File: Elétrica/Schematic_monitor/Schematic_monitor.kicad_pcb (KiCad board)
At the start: 2 copper layers, 49 parts, among them J1 Conn_01x04, J2 USB_B_Micro, J3 Eletrode 1, J4 Eletrode 2, SW1 SW_Push, SW2 SW_SPDT, SW3 SW_SPDT, SW4 SW_SPDT, SW5 SW_SPDT, SW6 SW_SPDT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

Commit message: Temp sensor
Adicionado sensor de temperatura
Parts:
- removed SW3, SW4, SW5, SW6, SW7: SW_SPDT, Button_Switch_SMD:SW_DIP_SPSTx01_Slide_9.78x4.72mm_W8.61mm_P2.54mm
- removed U3: EA_eDIPTFT32-A, Display:EA_eDIPTFT32-XXX
- C15: footprint Capacitor_SMD:C_Elec_3x5.4 -> Capacitor_SMD:C_0603_1608Metric_Pad1.08x0.95mm_HandSolder
- FB1, FB3: value FerriteBead -> New_Library:FerriteBead; footprint Inductor_SMD:L_0603_1608Metric -> Inductor_SMD:L_0603_1608Metric_Pad1.05x0.95mm_HandSolder
- FB2: footprint Inductor_SMD:L_0603_1608Metric -> Inductor_SMD:L_0603_1608Metric_Pad1.05x0.95mm_HandSolder
- moved U4 40.5 mm to (142.2, 91.4)
- moved D3 8.79 mm to (131.8, 119.0)
- moved C15 3.50 mm to (121.9, 123.2)
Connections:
- U1 pad 16: ADC1-2 -> unconnected-(U1-PA2-Pad16)
- U1 pad 41: unconnected-(U1-PA8-Pad41) -> I2C3_SCL
- U1 pad 42: unconnected-(U1-PA9-Pad42) -> I2C3_SDA
- U1 pad 58: unconnected-(U1-PB6-Pad58) -> I2C1_SCL
- U1 pad 59: unconnected-(U1-PB7-Pad59) -> I2C1_SDA
- U4 pad 2: unconnected-(U4-SCL-Pad2) -> I2C3_SCL
- U4 pad 3: unconnected-(U4-SDA-Pad3) -> I2C3_SDA

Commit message: sensor de temperatura
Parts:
- added C18: 0.1uF, Capacitor_SMD:C_0603_1608Metric, F.Cu at (159.4, 96.8)
- added U3: MLX90614ESF-ACC-000-TU, footprints:MLX90614xCC_MEL, F.Cu at (161.5, 87.8)
- D3: footprint Diode_SMD:D_PowerDI-5 -> Diode_SMD:D_0603_1608Metric
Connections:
- U1 pad 53: unconnected-(U1-PC12-Pad53) -> I2C1_SDA

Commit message: Atualizações
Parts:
- added U5: AD623, AD623:RM_8_ADI-L, F.Cu at (131.2, 103.2)
- added U6: LM358, LM358:D8-L, F.Cu at (138.3, 100.8)
- added U7: LM358, LM358:D8-L, F.Cu at (138.3, 107.3)
- added U8: LM358, LM358:D8-L, F.Cu at (138.3, 113.7)
- J3, J4: footprint Connector_PinHeader_1.00mm:PinHeader_1x01_P1.00mm_Horizontal -> Connector_PinHeader_2.54mm:PinHeader_1x01_P2.54mm_Vertical
- U3: footprint footprints:MLX90614xCC_MEL -> temp:MLX90614xCC_MEL
- U4: footprint oxy:21-0880B_MXM -> oximeter:21-0880B_MXM-L
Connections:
- net I2C1_SCL renamed scl_lcd
- C18 pad 1: VBUS -> GND
- C18 pad 2: GND -> VBUS
- J3 pad 1: Net-(J3-Pin_1) -> /EMG
- U1 pad 29: unconnected-(U1-PB10-Pad29) -> Temp_SCL
- U1 pad 41: I2C3_SCL -> oxi_scl
- U1 pad 42: I2C3_SDA -> oxi_sda
- U1 pad 53: I2C1_SDA -> Temp_SDA
- U1 pad 59: I2C1_SDA -> sda_lcd
- U3 pad 1: I2C3_SCL -> Temp_SCL
- U3 pad 2: I2C3_SDA -> Temp_SDA
- U3 pad 3: GND -> VBUS
- U4 pad 2: I2C3_SCL -> oxi_scl
- U4 pad 3: I2C3_SDA -> oxi_sda

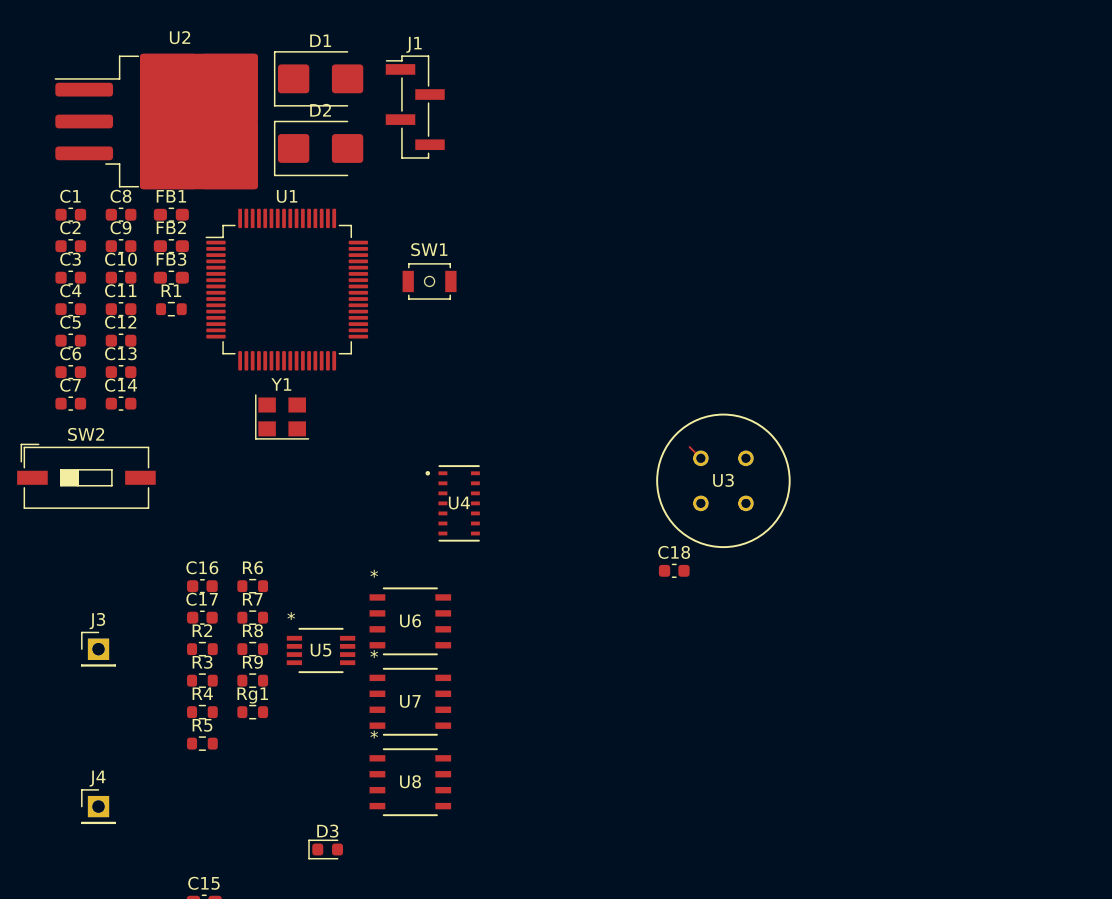
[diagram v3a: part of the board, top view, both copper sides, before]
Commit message: Versão PRJ2 e PRJ3 quase finalizada
Poucos detalhes precisam ser alterados para o envio dos trabalhos pelo menos do PRJ2. PRJ3 está finalizado
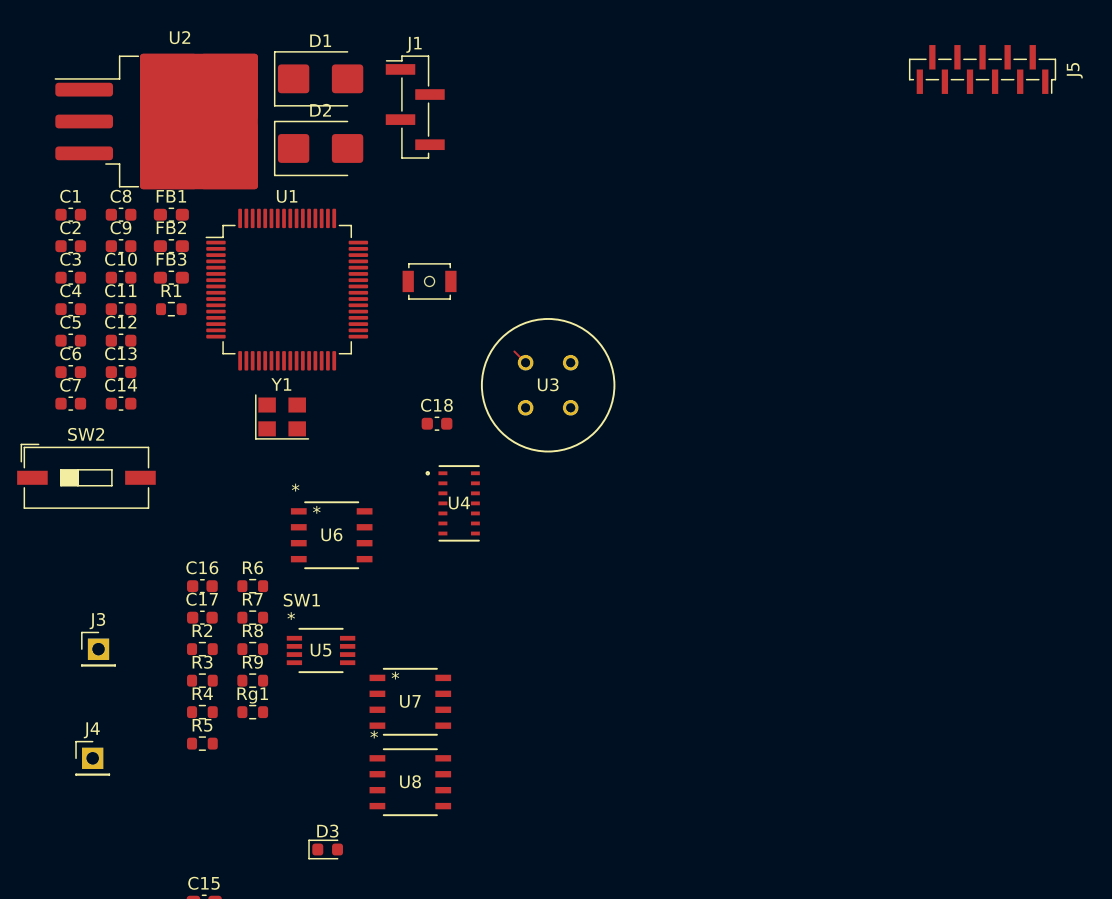
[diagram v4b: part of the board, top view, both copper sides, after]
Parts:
- added J5: Conn_01x11, Connector_PinSocket_1.00mm:PinSocket_1x11_P1.00mm_Vertical_SMD_Pin1Right, F.Cu at (184.0, 56.9)
- moved C18 22.3 mm to (140.5, 85.1)
- moved U3 15.9 mm to (147.5, 80.2)
- moved U6 9.30 mm to (132.1, 94.0)
- moved J4 3.88 mm to (113.0, 111.8)
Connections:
- U1 pad 14: ADC1-0 -> unconnected-(U1-PA0-Pad14)
- U1 pad 20: unconnected-(U1-PA4-Pad20) -> touch_int
- U1 pad 21: unconnected-(U1-PA5-Pad21) -> displ_sck
- U1 pad 22: unconnected-(U1-PA6-Pad22) -> touch_mosi
- U1 pad 23: unconnected-(U1-PA7-Pad23) -> displ_mosi
- U1 pad 33: unconnected-(U1-PB12-Pad33) -> displ_cs
- U1 pad 34: unconnected-(U1-PB13-Pad34) -> touch_cs
- U1 pad 35: unconnected-(U1-PB14-Pad35) -> displ_dc
- U1 pad 36: unconnected-(U1-PB15-Pad36) -> displ_rst
- U1 pad 38: unconnected-(U1-PC7-Pad38) -> displ_led

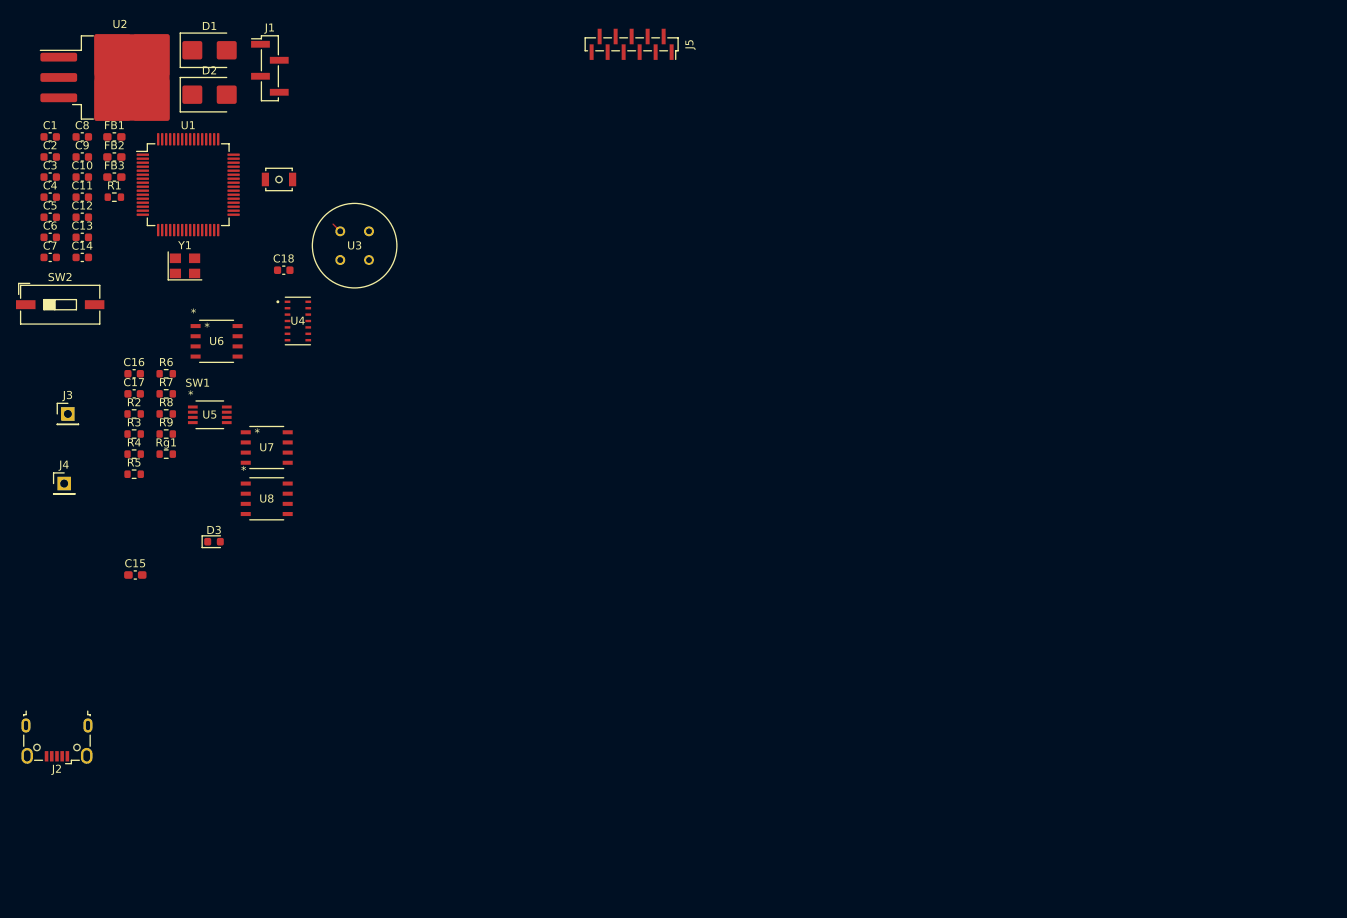
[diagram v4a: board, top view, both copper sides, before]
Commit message: Final Detalis to  PRJ2
Added final detalis in PCB desing and STM32 configuration.
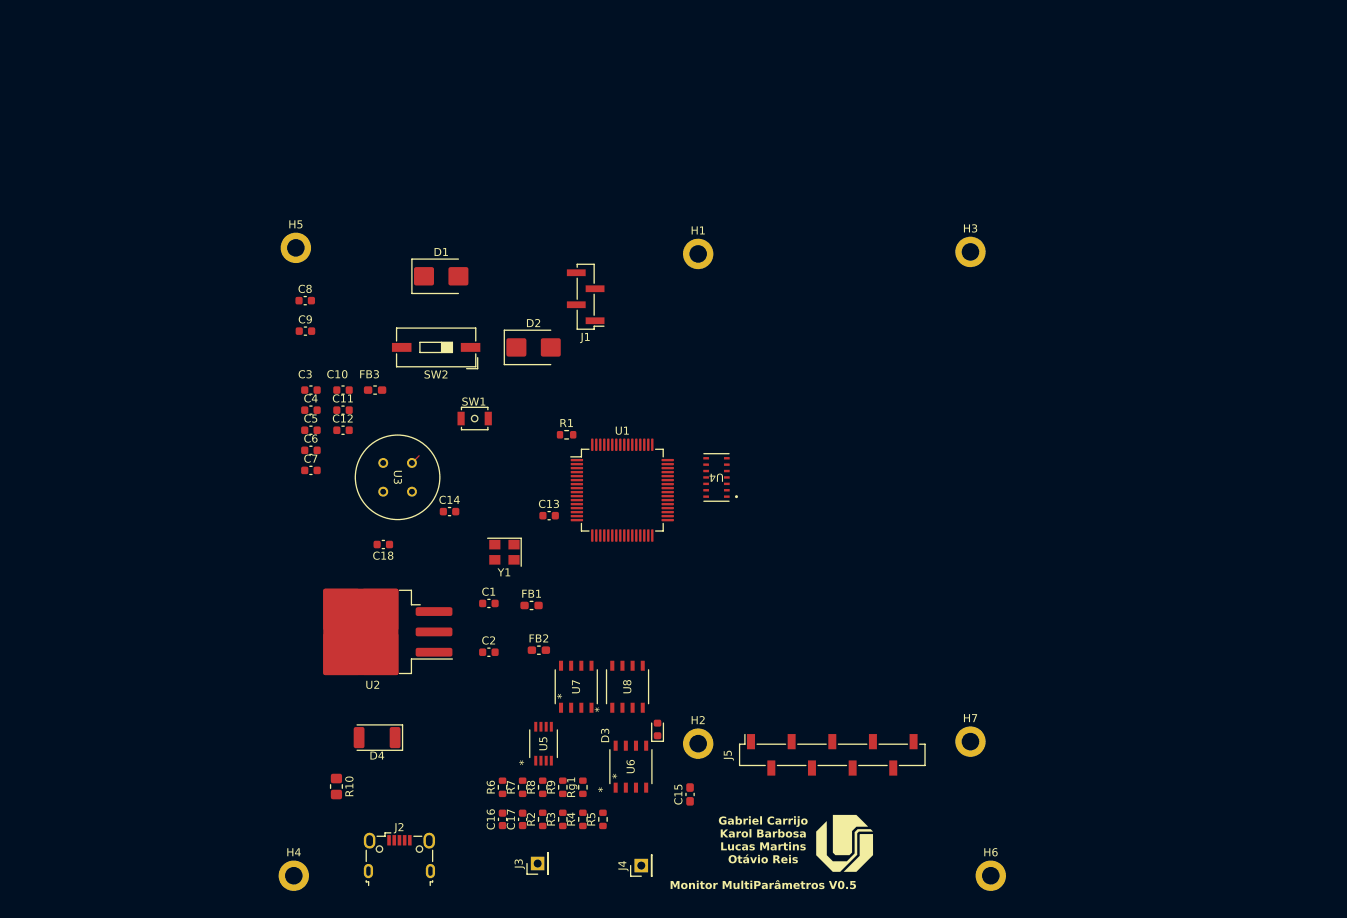
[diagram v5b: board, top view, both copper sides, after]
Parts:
- added D4: LED, LED_SMD:LED_2010_5025Metric, F.Cu at (152.1, 143.5)
- added G***: LOGO, UFU_bitmapfile:UFU_Bitmap, F.Cu at (210.6, 156.7)
- added H1: MountingHole_Pad, MountingHole:MountingHole_2.2mm_M2_DIN965_Pad, F.Cu at (192.3, 83.1)
- added H2: MountingHole_Pad, MountingHole:MountingHole_2.2mm_M2_DIN965_Pad, F.Cu at (192.3, 144.3)
- added H3: MountingHole_Pad, MountingHole:MountingHole_2.2mm_M2_DIN965_Pad, F.Cu at (226.3, 82.8)
- added H4: MountingHole_Pad, MountingHole:MountingHole_2.2mm_M2_DIN965_Pad, F.Cu at (141.7, 160.8)
- added H5: MountingHole_Pad, MountingHole:MountingHole_2.2mm_M2_DIN965_Pad, F.Cu at (142.0, 82.3)
- added H6: MountingHole_Pad, MountingHole:MountingHole_2.2mm_M2_DIN965_Pad, F.Cu at (228.9, 160.8)
- added H7: MountingHole_Pad, MountingHole:MountingHole_2.2mm_M2_DIN965_Pad, F.Cu at (226.3, 144.0)
- added R10: 100, Resistor_SMD:R_0805_2012Metric_Pad1.20x1.40mm_HandSolder, F.Cu at (147.1, 149.6)
- J5: value Conn_01x11 -> Conn_01x09; footprint Connector_PinSocket_1.00mm:PinSocket_1x11_P1.00mm_Vertical_SMD_Pin1Right -> Connector_PinSocket_2.54mm:PinSocket_1x09_P2.54mm_Vertical_SMD_Pin1Right
- moved J5 92.3 mm to (209.0, 145.7), turned to 90 degrees
- moved J4 86.5 mm to (185.2, 159.5), turned to 90 degrees
- moved C2 82.7 mm to (166.1, 132.8)
- moved FB2 81.3 mm to (172.4, 132.6)
- moved J3 81.3 mm to (172.2, 159.3), turned to 90 degrees
- moved C1 80.0 mm to (166.1, 126.7)
- moved FB1 78.4 mm to (171.4, 127.0)
- moved U2 76.2 mm to (151.6, 130.3), turned to 180 degrees
- moved C15 74.6 mm to (191.3, 150.6), turned to 90 degrees
- moved U6 74.2 mm to (183.9, 147.1), turned to 90 degrees
- moved R5 72.8 mm to (180.4, 153.7), turned to 90 degrees
- moved R4 72.3 mm to (177.9, 153.7), turned to 90 degrees
- moved C16 72.3 mm to (167.8, 153.7), turned to 90 degrees
- moved R3 72.0 mm to (175.4, 153.7), turned to 90 degrees
- moved C17 72.0 mm to (170.3, 153.7), turned to 90 degrees
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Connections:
- C15 pad 1: Net-(C15-Pad1) -> ADC1-1
- C15 pad 2: Net-(U7A-+) -> ADC1-1
- C16 pad 1: Net-(C16-Pad1) -> ADC1-1
- C16 pad 2: Vref -> ADC1-1
- C17 pad 1: Net-(C16-Pad1) -> ADC1-1
- C17 pad 2: Net-(U8A--) -> ADC1-1
- J3 pad 1: /EMG -> ADC1-1
- J4 pad 1: Net-(J4-Pin_1) -> ADC1-1
- J5 pad 1: GND -> displ_led
- J5 pad 2: displ_led -> displ_rst
- J5 pad 3: displ_rst -> displ_dc
- J5 pad 4: displ_dc -> touch_cs
- J5 pad 5: touch_cs -> displ_cs
- J5 pad 6: displ_cs -> displ_mosi
- J5 pad 7: displ_mosi -> touch_mosi
- J5 pad 8: touch_mosi -> displ_sck
- J5 pad 9: displ_sck -> touch_int
- R2 pad 2: Net-(U6A-+) -> ADC1-1
- R3 pad 1: Net-(U6A-+) -> ADC1-1
- R4 pad 1: Net-(U7A-+) -> ADC1-1
- R4 pad 2: Vref -> ADC1-1
- R5 pad 1: Net-(R5-Pad1) -> ADC1-1
- R5 pad 2: Net-(U7A--) -> ADC1-1
- R6 pad 1: Net-(U7A--) -> ADC1-1
- R7 pad 1: Net-(R5-Pad1) -> ADC1-1
- R7 pad 2: Net-(C16-Pad1) -> ADC1-1
- R8 pad 1: Net-(C16-Pad1) -> ADC1-1
- R8 pad 2: Net-(U8A-+) -> ADC1-1
- R9 pad 1: Net-(U8A--) -> ADC1-1
- Rg1 pad 1: Net-(Rg1-Pad1) -> ADC1-1
- U5 pad 1: Net-(Rg1-Pad1) -> ADC1-1
- U5 pad 2: /EMG -> ADC1-1
- U5 pad 3: Net-(J4-Pin_1) -> ADC1-1
- U5 pad 5: Vref -> ADC1-1
- U5 pad 6: Net-(C15-Pad1) -> ADC1-1
- U6 pad 1: Vref -> ADC1-1
- U6 pad 2: Vref -> ADC1-1
- U6 pad 3: Net-(U6A-+) -> ADC1-1
- U7 pad 1: Net-(R5-Pad1) -> ADC1-1
- U7 pad 2: Net-(U7A--) -> ADC1-1
- U7 pad 3: Net-(U7A-+) -> ADC1-1
- U8 pad 1: Net-(U8A--) -> ADC1-1
- U8 pad 2: Net-(U8A--) -> ADC1-1
- U8 pad 3: Net-(U8A-+) -> ADC1-1
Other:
- board text added: "Gabriel Carrijo Karol Barbosa Lucas Martins Otávio Reis Monitor MultiParâmetros V0.5"

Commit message: Inicio PRJ4
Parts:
- D1, D2: footprint Diode_SMD:D_SMB -> Diode_SMD:D_0603_1608Metric_Pad1.05x0.95mm_HandSolder
- H2: value MountingHole_Pad -> ~
- moved J2 81.5 mm to (183.1, 81.7)
- moved D4 75.1 mm to (226.8, 150.8)
- moved R10 74.3 mm to (221.4, 151.1)
- moved U2 60.0 mm to (208.1, 110.1)
- moved U4 49.3 mm to (185.9, 159.6), turned to 0 degrees
- moved Y1 41.4 mm to (207.2, 133.7)
- moved U7 36.8 mm to (143.5, 152.4), turned to 180 degrees
- moved R5 35.7 mm to (144.8, 156.5), turned to 180 degrees
- moved C13 35.1 mm to (206.7, 127.6)
- moved C15 34.2 mm to (157.2, 153.6)
- moved U6 33.6 mm to (153.0, 160.3), turned to 0 degrees
- moved D3 31.7 mm to (155.5, 142.8), turned to 0 degrees
- moved U8 29.7 mm to (155.4, 147.1), turned to 0 degrees
- moved FB1 28.7 mm to (200.1, 129.5)
- moved FB2 28.7 mm to (201.0, 135.1)
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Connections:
- C15 pad 1: ADC1-1 -> Net-(C15-Pad1)
- C15 pad 2: ADC1-1 -> Net-(U7A-+)
- C16 pad 1: ADC1-1 -> Net-(C16-Pad1)
- C16 pad 2: ADC1-1 -> Vref
- C17 pad 1: ADC1-1 -> Net-(C16-Pad1)
- C17 pad 2: ADC1-1 -> Net-(U8A--)
- J3 pad 1: ADC1-1 -> Net-(J3-Pin_1)
- J4 pad 1: ADC1-1 -> Net-(J4-Pin_1)
- R2 pad 2: ADC1-1 -> Net-(U6A-+)
- R3 pad 1: ADC1-1 -> GND
- R4 pad 1: ADC1-1 -> Net-(U7A-+)
- R4 pad 2: ADC1-1 -> Vref
- R5 pad 1: ADC1-1 -> Net-(R5-Pad1)
- R5 pad 2: ADC1-1 -> Net-(U7A--)
- R6 pad 1: ADC1-1 -> Net-(U7A--)
- R7 pad 1: ADC1-1 -> Net-(R5-Pad1)
- R7 pad 2: ADC1-1 -> Net-(C16-Pad1)
- R8 pad 1: ADC1-1 -> Net-(C16-Pad1)
- R8 pad 2: ADC1-1 -> Net-(U8A-+)
- R9 pad 1: ADC1-1 -> Net-(U8A--)
- Rg1 pad 1: ADC1-1 -> Net-(Rg1-Pad1)
- U1 pad 40: unconnected-(U1-PC9-Pad40) -> oxi_sda
- U1 pad 42: oxi_sda -> unconnected-(U1-PA9-Pad42)
- U1 pad 58: scl_lcd -> unconnected-(U1-PB6-Pad58)
- U1 pad 59: sda_lcd -> unconnected-(U1-PB7-Pad59)
- U5 pad 1: ADC1-1 -> Net-(Rg1-Pad1)
- U5 pad 2: ADC1-1 -> Net-(J3-Pin_1)
- U5 pad 3: ADC1-1 -> Net-(J4-Pin_1)
- U5 pad 5: ADC1-1 -> Vref
- U5 pad 6: ADC1-1 -> Net-(C15-Pad1)
- U6 pad 1: ADC1-1 -> Vref
- U6 pad 2: ADC1-1 -> Vref
- U6 pad 3: ADC1-1 -> Net-(U6A-+)
- U7 pad 1: ADC1-1 -> Net-(R5-Pad1)
- U7 pad 2: ADC1-1 -> Net-(U7A--)
- U7 pad 3: ADC1-1 -> Net-(U7A-+)
- U8 pad 1: ADC1-1 -> Net-(U8A--)
- U8 pad 2: ADC1-1 -> Net-(U8A--)
- U8 pad 3: ADC1-1 -> Net-(U8A-+)
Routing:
- net ADC1-1: track 0.00 -> 38.9 mm
- net Net-(J4-Pin_1): track 0.00 -> 17.0 mm
- net Net-(U7A-+): track 0.00 -> 13.1 mm, vias 0 -> 1
- net Net-(J3-Pin_1): track 0.00 -> 13.1 mm
- net Net-(C16-Pad1): track 0.00 -> 12.5 mm
- net Net-(U8A--): track 0.00 -> 11.9 mm
- net Net-(Rg1-Pad1): track 0.00 -> 10.2 mm
- net Net-(U7A--): track 0.00 -> 10.1 mm, vias 0 -> 1
- net Net-(Rg1-Pad2): track 0.00 -> 9.79 mm
- net Vref: track 0.00 -> 5.69 mm
- net Net-(C15-Pad1): track 0.00 -> 5.10 mm
- net Net-(R5-Pad1): track 0.00 -> 4.62 mm
- net Net-(U6A-+): track 0.00 -> 4.30 mm
- net Net-(U8A-+): track 0.00 -> 3.87 mm
- net GND: track 0.00 -> 1.60 mm
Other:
- copper layers 2 -> 4

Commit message: PRJ4
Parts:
- moved C3 115.0 mm to (256.3, 76.3)
- moved C4 115.0 mm to (256.3, 78.8)
- moved C5 115.0 mm to (256.3, 81.3)
- moved C6 114.4 mm to (256.6, 88.6)
- moved C7 114.4 mm to (256.6, 91.1)
- moved C8 113.8 mm to (256.7, 96.3)
- moved C9 113.8 mm to (256.7, 100.7)
- moved J1 102.9 mm to (269.0, 109.9)
- moved SW2 97.4 mm to (255.0, 113.9), turned to 0 degrees
- moved C10 94.4 mm to (237.6, 70.6)
- moved C11 94.4 mm to (237.6, 73.1)
- moved C12 94.4 mm to (237.6, 75.6)
- moved C18 94.4 mm to (242.6, 89.9)
- moved FB3 94.4 mm to (241.6, 70.6)
- moved D1 94.1 mm to (251.6, 108.2), turned to 180 degrees
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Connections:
- J2 pad 2: USB_D- -> USB_D+
- J2 pad 3: USB_D+ -> USB_D-
- R3 pad 1: GND -> Net-(U6A-+)
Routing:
- net VBUS: track 0.00 -> 122.7 mm, vias 0 -> 9
- net GND: track 1.60 -> 79.2 mm, vias 0 -> 6
- net USB_D-: track 0.00 -> 42.3 mm
- net USB_D+: track 0.00 -> 42.2 mm
- net ADC1-1: track 38.9 -> 7.35 mm
- net Net-(U2-VO): track 0.00 -> 26.7 mm
- net Vref: track 5.69 -> 29.0 mm
- net Net-(D4-A): track 0.00 -> 3.73 mm
- added copper zone on In1.Cu, net GND
- added copper zone on In2.Cu, net VBUS

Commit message: PRJ4
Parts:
- added R11: 3k, Resistor_SMD:R_0603_1608Metric, F.Cu at (141.1, 131.1)
- added R12: 3k, Resistor_SMD:R_0603_1608Metric, F.Cu at (143.5, 131.1)
- added R13: 4.7k, Resistor_SMD:R_0603_1608Metric, F.Cu at (175.2, 147.8)
- added R14: 4.7k, Resistor_SMD:R_0603_1608Metric, F.Cu at (161.9, 148.2)
- moved J1 111.8 mm to (157.5, 101.9), turned to 0 degrees
- moved SW1 109.0 mm to (143.3, 115.0), turned to 90 degrees
- moved D1 103.8 mm to (148.0, 115.0), turned to -90 degrees
- moved Y1 95.3 mm to (164.6, 114.1), turned to 0 degrees
- moved C12 94.5 mm to (151.6, 114.9), turned to -90 degrees
- moved C13 93.7 mm to (165.3, 110.2), turned to 180 degrees
- moved U3 88.1 mm to (170.5, 149.3)
- moved C18 85.7 mm to (173.6, 140.8), turned to 0 degrees
- moved SW2 85.3 mm to (170.8, 99.7), turned to 90 degrees
- moved C14 78.6 mm to (168.7, 111.1), turned to -90 degrees
- moved R1 77.5 mm to (184.2, 99.2)
- moved C3 73.1 mm to (191.1, 109.3), turned to 90 degrees
- moved D2 71.9 mm to (177.9, 99.9), turned to -90 degrees
- moved C5 70.5 mm to (188.8, 101.4), turned to -90 degrees
- moved C4 69.8 mm to (193.6, 109.3), turned to 90 degrees
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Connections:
- H6 pad 1: GND -> unconnected-(H6-Pad1)
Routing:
- net GND: track 79.2 -> 380.3 mm, vias 6 -> 18
- net +3.3V: track 0.00 -> 173.4 mm, vias 0 -> 2
- net +3.3VA: track 0.00 -> 75.8 mm, vias 0 -> 7
- net displ_sck: track 0.00 -> 61.8 mm, vias 0 -> 3
- net displ_cs: track 0.00 -> 61.6 mm, vias 0 -> 2
- net touch_int: track 0.00 -> 61.0 mm, vias 0 -> 3
- net displ_mosi: track 0.00 -> 59.4 mm, vias 0 -> 3
- net touch_mosi: track 0.00 -> 56.5 mm, vias 0 -> 3
- net displ_dc: track 0.00 -> 54.0 mm, vias 0 -> 2
- net touch_cs: track 0.00 -> 53.9 mm, vias 0 -> 2
- net ADC1-1: track 7.35 -> 57.2 mm, vias 0 -> 1
- net oxi_scl: track 0.00 -> 49.8 mm, vias 0 -> 1
- net Temp_SDA: track 0.00 -> 47.3 mm, vias 0 -> 1
- net NRST: track 0.00 -> 47.0 mm, vias 0 -> 2
- net oxi_sda: track 0.00 -> 46.3 mm
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- removed copper zone on In1.Cu, net GND
- removed copper zone on In2.Cu, net VBUS
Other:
- board outline added: 91.9 x 78.7 mm
